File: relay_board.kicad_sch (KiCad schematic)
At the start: 0 parts

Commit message: Add relay board schematic
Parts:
- added D1, D2, D3, D4: D, symbol Device:D
- added J3: J_PRECURSOR_A, symbol Connector_Generic:Conn_01x02
- added J6: J_FORELINE_VALVE, symbol Connector_Generic:Conn_01x02
- added J7: J_N2_PURGE, symbol Connector_Generic:Conn_01x02
- added J8: J_SPARE, symbol Connector_Generic:Conn_01x02
- added K1: Relay 2, symbol Relay:Relay_SPST-NO
- added K2: Relay 1, symbol Relay:Relay_SPST-NO
- added K3: Relay 3, symbol Relay:Relay_SPST-NO
- added K4: Relay 4, symbol Relay:Relay_SPST-NO
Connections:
- new net: J6.1 (Pin_1), K2.14
- new net: J8.1 (Pin_1), K4.14
- new net: J7.1 (Pin_1), K3.14
- new net: J3.1 (Pin_1), K1.14
- new net +12V: D2.1 (K), K2.13, K2.A1
- new net +24V: D1.1 (K), D3.1 (K), D4.1 (K), K1.13, K1.A1, K3.13, K3.A1, K4.13, K4.A1
- new net GNDPWR: J3.2 (Pin_2), J6.2 (Pin_2), J7.2 (Pin_2), J8.2 (Pin_2)
- new net P0.0: D2.2 (A), K2.A2
- new net P0.1: D1.2 (A), K1.A2
- new net P0.2: D3.2 (A), K3.A2
- new net P0.3: D4.2 (A), K4.A2

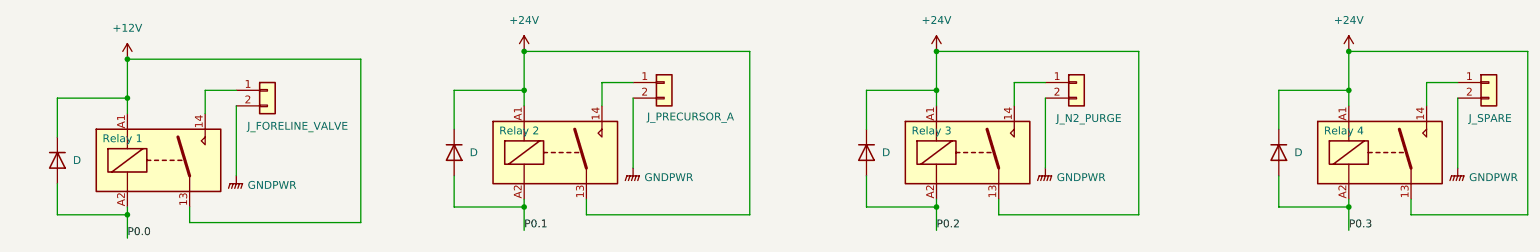
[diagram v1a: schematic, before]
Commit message: fix ERC errors in relay board schematic
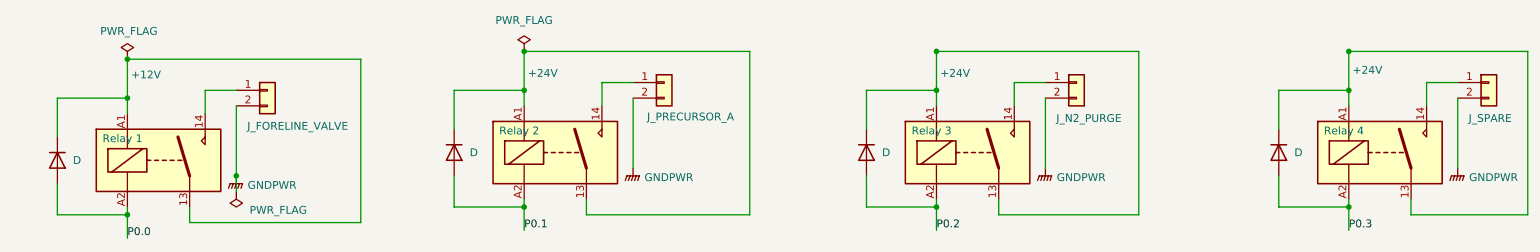
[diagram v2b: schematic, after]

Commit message: fixed GND and diodes on the relay board
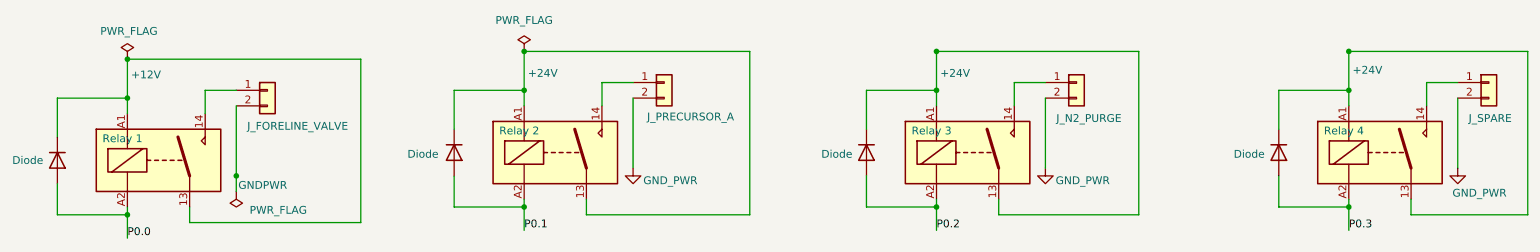
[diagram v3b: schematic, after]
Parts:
- D1, D2, D3, D4: value D -> Diode
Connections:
- net GNDPWR: no longer J3.2 (Pin_2), J7.2 (Pin_2), J8.2 (Pin_2)
- new net GND_PWR: J3.2 (Pin_2), J7.2 (Pin_2), J8.2 (Pin_2)
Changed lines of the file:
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@@
 	)
 	(symbol
+		(lib_id "power:GND")
+		(at 120.65 87.63 0)
+		(unit 1)
+		(exclude_from_sim no)
+		(in_bom yes)
+		(on_board yes)
+		(dnp no)
+		(property "Reference" "#PWR018"
+			(at 120.65 93.98 0)
+			(effects
+				(font
+					(size 1.27 1.27)
+				)
+				(hide yes)
+			)
+		)
+		(property "Value" "GND_PWR"
+			(at 126.746 89.662 0)
+			(effects
+				(font
+					(size 1.27 1.27)
+				)
+			)
+		)
+		(property "Footprint" ""
+			(at 120.65 87.63 0)
+			(effects
+				(font
+					(size 1.27 1.27)
+				)
+				(hide yes)
+			)
+		)
+		(property "Datasheet" ""
+			(at 120.65 87.63 0)
+			(effects
+				(font
+					(size 1.27 1.27)
+				)
+				(hide yes)
+			)
+		)
+		(property "Description" "Power symbol creates a global label with name \"GND\" , ground"
+			(at 120.65 87.63 0)
+			(effects
+				(font
+					(size 1.27 1.27)
+				)
+				(hide yes)
+			)
+		)
+		(pin "1"
+		)
+		(instances
+			(project ""
+				(path "/0db39e9c-e7a7-46b4-b6c2-b1f3e7389c4f/f7c6a359-8623-4d62-a80b-5dc912748245"
+					(reference "#PWR018")
+					(unit 1)
+				)
+			)
+		)
+	)
+	(symbol
+		(lib_name "GNDPWR_1")
 		(lib_id "power:GNDPWR")
 		(at 55.88 88.9 0)
@@
 		)
 		(property "Value" "GNDPWR"
-			(at 61.722 90.424 0)
+			(at 60.198 90.424 0)
 			(effects
 				(font
@@
 	)
 	(symbol
-		(lib_id "power:GNDPWR")
-		(at 120.65 87.63 0)
-		(unit 1)
-		(exclude_from_sim no)
-		(in_bom yes)
-		(on_board yes)
-		(dnp no)
-		(property "Reference" "#PWR018"
-			(at 120.65 92.71 0)
-			(effects
-				(font
-					(size 1.27 1.27)
-				)
-				(hide yes)
-			)
-		)
-		(property "Value" "GNDPWR"
-			(at 126.492 89.154 0)
-			(effects
-				(font
-					(size 1.27 1.27)
-				)
-			)
-		)
-		(property "Footprint" ""
-			(at 120.65 88.9 0)
-			(effects
-				(font
-					(size 1.27 1.27)
-				)
-				(hide yes)
-			)
-		)
-		(property "Datasheet" ""
-			(at 120.65 88.9 0)
-			(effects
-				(font
-					(size 1.27 1.27)
-				)
-				(hide yes)
-			)
-		)
-		(property "Description" "Power symbol creates a global label with name \"GNDPWR\" , global ground"
-			(at 120.65 87.63 0)
-			(effects
-				(font
-					(size 1.27 1.27)
-				)
-				(hide yes)
-			)
-		)
-		(pin "1"
-		)
-		(instances
-			(project ""
-				(path "/0db39e9c-e7a7-46b4-b6c2-b1f3e7389c4f/f7c6a359-8623-4d62-a80b-5dc912748245"
-					(reference "#PWR018")
-					(unit 1)
-				)
-			)
-		)
-	)
-	(symbol
 		(lib_id "Device:D")
 		(at 158.75 85.09 270)
@@
 		(on_board yes)
 		(dnp no)
-		(fields_autoplaced yes)
 		(property "Reference" "D3"
 			(at 161.29 83.8199 90)
@@
 			)
 		)
-		(property "Value" "D"
-			(at 161.29 85.0899 90)
+		(property "Value" "Diode"
+			(at 151.384 85.344 90)
 			(effects
 				(font
@@
 				(path "/0db39e9c-e7a7-46b4-b6c2-b1f3e7389c4f/f7c6a359-8623-4d62-a80b-5dc912748245"
 					(reference "D3")
+					(unit 1)
+				)
+			)
+		)
+	)
+	(symbol
+		(lib_id "power:GND")
+		(at 187.96 87.63 0)
+		(unit 1)
+		(exclude_from_sim no)
+		(in_bom yes)
+		(on_board yes)
+		(dnp no)
+		(property "Reference" "#PWR022"
+			(at 187.96 93.98 0)
+			(effects
+				(font
+					(size 1.27 1.27)
+				)
+				(hide yes)
+			)
+		)
+		(property "Value" "GND_PWR"
+			(at 194.056 89.662 0)
+			(effects
+				(font
+					(size 1.27 1.27)
+				)
+			)
+		)
+		(property "Footprint" ""
+			(at 187.96 87.63 0)
+			(effects
+				(font
+					(size 1.27 1.27)
+				)
+				(hide yes)
+			)
+		)
+		(property "Datasheet" ""
+			(at 187.96 87.63 0)
+			(effects
+				(font
+					(size 1.27 1.27)
+				)
+				(hide yes)
+			)
+		)
+		(property "Description" "Power symbol creates a global label with name \"GND\" , ground"
+			(at 187.96 87.63 0)
+			(effects
+				(font
+					(size 1.27 1.27)
+				)
+				(hide yes)
+			)
+		)
+		(pin "1"
+		)
+		(instances
+			(project ""
+				(path "/0db39e9c-e7a7-46b4-b6c2-b1f3e7389c4f/f7c6a359-8623-4d62-a80b-5dc912748245"
+					(reference "#PWR022")
 					(unit 1)
 				)
@@
 	)
 	(symbol
-		(lib_id "power:GNDPWR")
+		(lib_id "power:GND")
 		(at 255.27 87.63 0)
 		(unit 1)
@@
 		(dnp no)
 		(property "Reference" "#PWR024"
-			(at 255.27 92.71 0)
-			(effects
-				(font
-					(size 1.27 1.27)
-				)
-				(hide yes)
-			)
-		)
-		(property "Value" "GNDPWR"
-			(at 261.112 89.154 0)
-			(effects
-				(font
-					(size 1.27 1.27)
-				)
-			)
-		)
-		(property "Footprint" ""
-			(at 255.27 88.9 0)
+			(at 255.27 93.98 0)
+			(effects
+				(font
+					(size 1.27 1.27)
+				)
+				(hide yes)
+			)
+		)
+		(property "Value" "GND_PWR"
+			(at 258.826 91.694 0)
+			(effects
+				(font
+					(size 1.27 1.27)
+				)
+			)
+		)
+		(property "Footprint" ""
+			(at 255.27 87.63 0)
 			(effects
 				(font
@@
 		)
 		(property "Datasheet" ""
-			(at 255.27 88.9 0)
-			(effects
-				(font
-					(size 1.27 1.27)
-				)
-				(hide yes)
-			)
-		)
-		(property "Description" "Power symbol creates a global label with name \"GNDPWR\" , global ground"
 			(at 255.27 87.63 0)
 			(effects
@@
 			)
 		)
-		(pin "1"
-		)
-		(instances
-			(project "ald_control_board"
+		(property "Description" "Power symbol creates a global label with name \"GND\" , ground"
+			(at 255.27 87.63 0)
+			(effects
+				(font
+					(size 1.27 1.27)
+				)
+				(hide yes)
+			)
+		)
+		(pin "1"
+		)
+		(instances
+			(project ""
 				(path "/0db39e9c-e7a7-46b4-b6c2-b1f3e7389c4f/f7c6a359-8623-4d62-a80b-5dc912748245"
 					(reference "#PWR024")
@@
 		(on_board yes)
 		(dnp no)
-		(fields_autoplaced yes)
 		(property "Reference" "D4"
 			(at 228.6 83.8199 90)
@@
 			)
 		)
-		(property "Value" "D"
-			(at 228.6 85.0899 90)
+		(property "Value" "Diode"
+			(at 218.694 85.344 90)
 			(effects
 				(font
@@
 		(on_board yes)
 		(dnp no)
-		(fields_autoplaced yes)
 		(property "Reference" "D1"
 			(at 93.98 83.8199 90)
@@
 			)
 		)
-		(property "Value" "D"
-			(at 93.98 85.0899 90)
+		(property "Value" "Diode"
+			(at 83.82 85.344 90)
 			(effects
 				(font
@@
 		(on_board yes)
 		(dnp no)
-		(fields_autoplaced yes)
 		(property "Reference" "D2"
 			(at 29.21 85.0899 90)
@@
 			)
 		)
-		(property "Value" "D"
-			(at 29.21 86.3599 90)
+		(property "Value" "Diode"
+			(at 19.304 86.36 90)
 			(effects
 				(font
@@
 					(unit 1)
 				)
-			)
-		)
-	)
-	(symbol
-		(lib_id "power:GNDPWR")
-		(at 187.96 87.63 0)
-		(unit 1)
-		(exclude_from_sim no)
-		(in_bom yes)
-		(on_board yes)
-		(dnp no)
-		(property "Reference" "#PWR022"
-			(at 187.96 92.71 0)
-			(effects
-				(font
-					(size 1.27 1.27)
-				)
-				(hide yes)
-			)
-		)
-		(property "Value" "GNDPWR"
-			(at 193.802 89.154 0)
-			(effects
-				(font
-					(size 1.27 1.27)
-				)
-			)
-		)
-		(property "Footprint" ""
-			(at 187.96 88.9 0)
-			(effects
-				(font
-					(size 1.27 1.27)
-				)
-				(hide yes)
-			)
-		)
-		(property "Datasheet" ""
-			(at 187.96 88.9 0)
-			(effects
-				(font
-					(size 1.27 1.27)
-				)
-				(hide yes)
-			)
-		)
-		(property "Description" "Power symbol creates a global label with name \"GNDPWR\" , global ground"
-			(at 187.96 87.63 0)
-			(effects
-				(font
-					(size 1.27 1.27)
-				)
-				(hide yes)
-			)
-		)
-		(pin "1"
-		)
-		(instances
-			(project "ald_control_board"
-				(path "/0db39e9c-e7a7-46b4-b6c2-b1f3e7389c4f/f7c6a359-8623-4d62-a80b-5dc912748245"
-					(reference "#PWR022")
-					(unit 1)
-				)
